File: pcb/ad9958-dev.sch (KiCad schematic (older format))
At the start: 120 parts, among them J1 5V, J2 HEAD-M10X2, J3 OUT0p, J4 OUT0n,1p, J5 15V, Q1 BFS17W, Q2 BFS17W, Q3 BFS17W, Q4 BFS17W, U1 LD1117V33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

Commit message: More schematic work - should be ready for layout
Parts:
- removed C31, C33, C34, C35, C40, C41, C42, C44, C48, C49, C50, C53, C54: 220n, IPC7351-Nominal:CAPC2012X70, symbol C-0805
- removed C39, C43, C45, C47, C51, C52: 1n, IPC7351-Nominal:CAPC1005X55, symbol C-0402
- removed C46: 47u, passive:C-ALUM-6.3mm, symbol C-ALUM-6.3mm
- removed D1: 1N5822, semi:DO-201, symbol 1N5822
- removed D2, D3: BAT54, IPC-semi-nominal:SOT-23, symbol BAT54
- removed E5, E6, E7, E8: 600, IPC7351-Nominal:INDC1005X60, symbol BEAD
- removed J2: HEAD-M10X2, conn:CONN_20-DIL, symbol HEAD-M10X2
- removed J5: 15V, conn:CONN_2-WIRES, symbol HEAD-M2
- removed JP1: SEL0n, conn:JUMPER-SOLDER-3, symbol JUMPER-SOLDER-3
- removed JP2: SEL1p, conn:JUMPER-SOLDER-3, symbol JUMPER-SOLDER-3
- removed MP1, MP2: 7-340-1PP-BA, symbol HEATSINK-NO-CONN
- removed Q1, Q2, Q3, Q4: BFS17W, IPC-semi-nominal:SOT-323, symbol BFS17W
- removed R15, R17: 220, IPC7351-Nominal:RESC1608X50, symbol R-0603
- removed R32: 3k3, IPC7351-Nominal:RESC1005X40, symbol R-0402
- removed R33: NP, IPC7351-Nominal:RESC1005X40, symbol R-0402
- removed R34, R35: 49r9, IPC7351-Nominal:RESC1005X40, symbol R-0402
- removed U1: LD1117V33, semi:TO-220, symbol LM1117-FIXED-TO220
- removed U2: LD1117V18, semi:TO-220, symbol LM1117-FIXED-TO220
- removed U4: LMV358, IPC7351-Nominal:SOP65P490X110-8B, symbol LMV358-MSOP
- added C31, C33, C35: 10n, symbol C-0402
- added C34: 100n, symbol C-0402
- added J2: 5V, symbol HEAD-F3
- added J5: HEAD-M10X2, symbol HEAD-M10X2
- added R15, R17: 49r9, symbol R-0402
- added U1: LM1117-FIXED-SOT223, symbol LM1117-FIXED-SOT223
- added U2, U4: LMH6714, symbol LMH6714-SOT23
- C29: value 1n -> 100n; footprint IPC7351-Nominal:CAPC1005X55 -> (none)
- C30, C36, C38: value 1n -> 10n; footprint IPC7351-Nominal:CAPC1005X55 -> (none)
- C32, C37: value 220n -> 10u; footprint IPC7351-Nominal:CAPC2012X70 -> (none)
- J1: value 5V -> 3V3
- J3: value OUT0p -> OUT0
- J4: value OUT0n,1p -> OUT1
- R13, R16: value 75 -> 49r9; footprint IPC7351-Nominal:RESC1005X40 -> (none)
- R18: value 360 -> 53r6; footprint IPC7351-Nominal:RESC1005X40 -> (none)
- R19: value 75 -> 53r6; footprint IPC7351-Nominal:RESC1005X40 -> (none)
- R20: value 3k3 -> 360; footprint IPC7351-Nominal:RESC1005X40 -> (none)
- R21: value 75 -> 360; footprint IPC7351-Nominal:RESC1005X40 -> (none)
- R22: value NP -> 360; footprint IPC7351-Nominal:RESC1005X40 -> (none)
- R23, R29, R30: value 10k -> 360; footprint IPC7351-Nominal:RESC1005X40 -> (none)
- R24: value 49r9 -> 2k2; footprint IPC7351-Nominal:RESC1005X40 -> (none)
- R25: value 10k -> 53r6; footprint IPC7351-Nominal:RESC1005X40 -> (none)
- R26: value 49r9 -> 53r6; footprint IPC7351-Nominal:RESC1005X40 -> (none)
- R27, R28: value 100 -> 360; footprint IPC7351-Nominal:RESC1005X40 -> (none)
- R31: value 360 -> 2k2; footprint IPC7351-Nominal:RESC1005X40 -> (none)
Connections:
- net labels added: +5, -5
- net labels removed: +15
- wire segments 334 -> 257
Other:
- note added: "4x 49r9"
- note added: "tline, Z0=50"
- note added: "tline, Z0=50, Zdiff=100"
- note removed: "75 OHM TLINE"
- moved on the sheet: J3

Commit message: PCB almost done
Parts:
- removed C11, C5: 47u, passive:C-ALUM-6.3mm, symbol C-ALUM-6.3mm
- removed C18, C26: 220n, IPC7351-Nominal:CAPC2012X70, symbol C-0805
- removed C33, C38: 10n, symbol C-0402
- removed J1: 3V3, conn:CONN_2-WIRES, symbol HEAD-M2
- added C33, C38: 10u, IPC7351-Nominal:CAPC2012X70, symbol C-0805
- added R32, R33: 49r9, IPC7351-Nominal:RESC1005X40, symbol R-0402
- C29, C30, C31, C34, C35, C36: footprint (none) -> IPC7351-Nominal:CAPC1005X55
- C32, C37: footprint (none) -> IPC7351-Nominal:CAPC2012X70
- J2: footprint (none) -> conn:CONN_3-SIL
- J5: footprint (none) -> conn:CONN_20-DIL
- R13, R15, R16, R17, R18, R19, R20, R21, R22, R23, R24, R25, R26, R27, R28, R29, R30, R31: footprint (none) -> IPC7351-Nominal:RESC1005X40
- U1: footprint (none) -> IPC-semi-nominal:SOT-223
- U2, U4: footprint (none) -> IPC-semi-nominal:SOT-23-5
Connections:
- net +1.8: no longer R13.1, R15.1, R16.1, R17.1, R18.1, R19.1, R25.1, R26.1
- net +1v8A: now also R13.1, R15.1, R16.1, R17.1, R18.1, R19.1, R25.1, R26.1
- net -5: now also C33.2, C38.2
- net GND: now also C33.1, C38.1
- net at R22.1, R24.1, U2.1 (OUT): now also R32.2; no longer J3.1
- net C0P: now reaches R25.2, R27.2
- net C0P: now also R13.2, U3.8 (CH0_IOUTp); no longer R16.2, U3.13 (CH1_IOUTp)
- net C0N: now reaches R26.2, R28.2
- net C0N: now also R15.2, U3.9 (CH0_IOUTn); no longer R17.2, U3.14 (CH2_IOUTn)
- net C1P: now reaches R18.2, R20.2
- net C1P: now also R16.2, U3.13 (CH1_IOUTp); no longer R13.2, U3.8 (CH0_IOUTp)
- net C1N: now reaches R19.2, R21.2
- net C1N: now also R17.2, U3.14 (CH2_IOUTn); no longer R15.2, U3.9 (CH0_IOUTn)
- net at E4.2: now also J5.20
- net at R1.2: now also J5.2; no longer J5.4
- net at R2.2: now also J5.16; no longer J5.6
- net at R3.2: now also J5.18; no longer J5.8
- net at R4.2: now also J5.4; no longer J5.10
- net at R5.2: now also J5.6; no longer J5.12
- net at R6.2: now also J5.8; no longer J5.14
- net at R7.2: now also J5.10; no longer J5.16
- net at R8.2: now also J5.12; no longer J5.18
- net at R9.2: now also J5.14; no longer J5.20
- net at R29.1, R31.1, U4.1 (OUT): now also R33.2; no longer J4.1
- new net: J3.1, R32.1
- new net: J4.1, R33.1
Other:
- note added: "tline, Z0=50, Zdiff=100\nOSH Park 4L: 0.3 track 0.7 space (1.0 align)"
- note removed: "tline, Z0=50, Zdiff=100"
- moved on the sheet: J3, J4, J5

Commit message: Added power protection, touched up PCB
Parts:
- added D1, D2, D3: SS12, IPC7351-Nominal:DIOM5326X292, symbol SS12
- added R34: 250mA, IPC7351-Nominal:RESC3216X60, symbol THERM
- added R35, R36: 100mA, IPC7351-Nominal:RESC3216X60, symbol THERM
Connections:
- net +3.3: now also D1.1, R34.2; no longer E4.1
- net +5: now also D2.1, R35.2; no longer E2.1
- net -5: now also D3.2, R36.2; no longer E3.1
- net GND: now also D1.2, D2.2, D3.1
- new net: E4.1, R34.1
- new net: E2.1, R35.1
- new net: E3.1, R36.1
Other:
- moved on the sheet: C12, C4, E2, E3, J2, U1

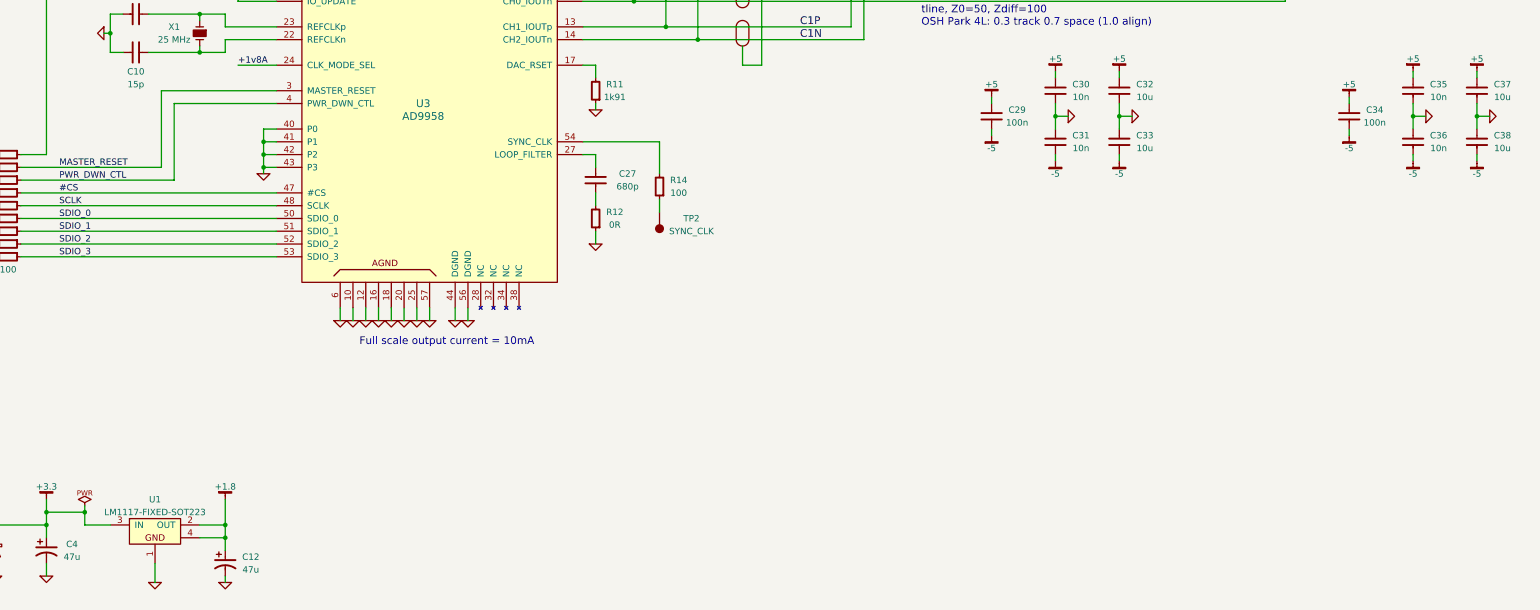
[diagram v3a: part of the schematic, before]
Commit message: Few part value changes
Added voltage to LDO
Changed 10nF to 1nF caps - eliminated BOM item
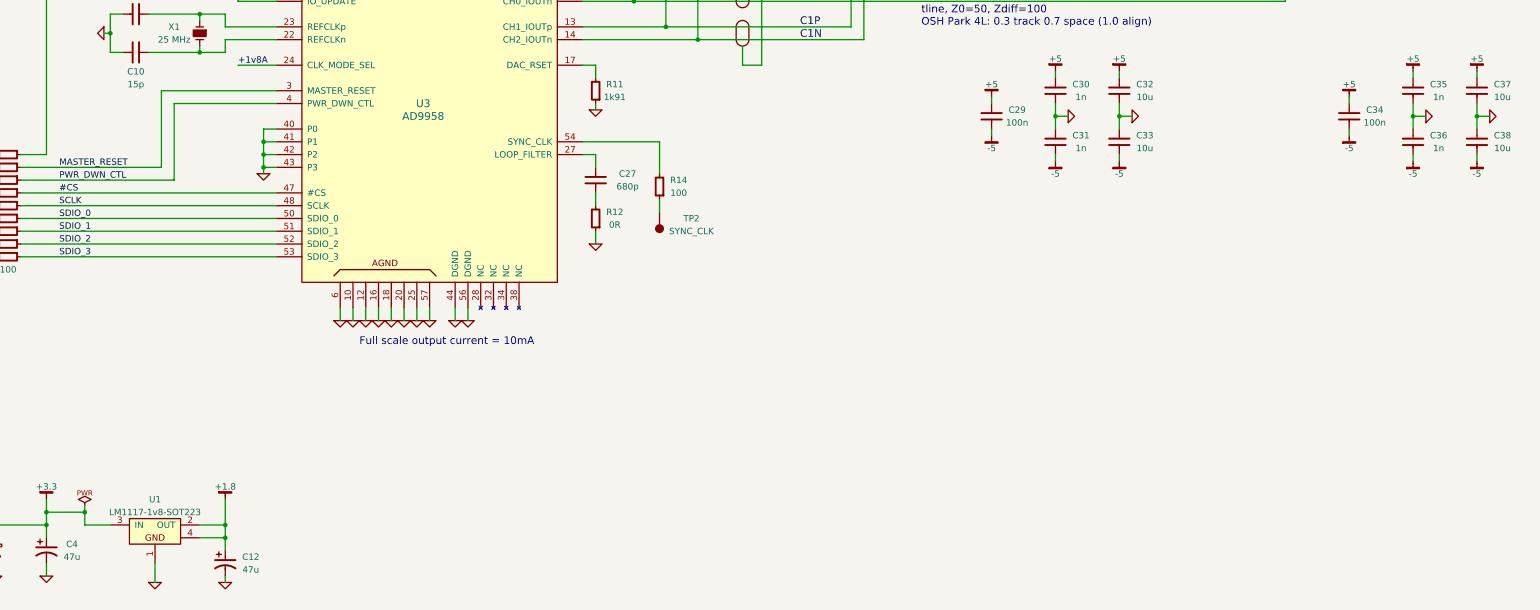
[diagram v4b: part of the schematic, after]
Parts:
- C30, C31, C35, C36: value 10n -> 1n
- U1: value LM1117-FIXED-SOT223 -> LM1117-1v8-SOT223
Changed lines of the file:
@@
 P 3350 8050
 F 0 "U1" H 3350 8300 50  0000 C CNN
-F 1 "LM1117-FIXED-SOT223" H 3350 8200 50  0000 C CNN
+F 1 "LM1117-1v8-SOT223" H 3350 8200 50  0000 C CNN
 F 2 "IPC-semi-nominal:SOT-223" H 3350 8050 60  0001 C CNN
 F 3 "" H 3350 8050 60  0000 C CNN
@@
 P 10400 4600
 F 0 "C30" H 10600 4650 50  0000 C CNN
-F 1 "10n" H 10600 4550 50  0000 C CNN
+F 1 "1n" H 10600 4550 50  0000 C CNN
 F 2 "IPC7351-Nominal:CAPC1005X55" H 10390 4575 60  0001 C CNN
 F 3 "" H 10390 4575 60  0000 C CNN
@@
 P 10400 5000
 F 0 "C31" H 10600 5050 50  0000 C CNN
-F 1 "10n" H 10600 4950 50  0000 C CNN
+F 1 "1n" H 10600 4950 50  0000 C CNN
 F 2 "IPC7351-Nominal:CAPC1005X55" H 10390 4975 60  0001 C CNN
 F 3 "" H 10390 4975 60  0000 C CNN
@@
 P 13200 4600
 F 0 "C35" H 13400 4650 50  0000 C CNN
-F 1 "10n" H 13400 4550 50  0000 C CNN
+F 1 "1n" H 13400 4550 50  0000 C CNN
 F 2 "IPC7351-Nominal:CAPC1005X55" H 13190 4575 60  0001 C CNN
 F 3 "" H 13190 4575 60  0000 C CNN
@@
 P 13200 5000
 F 0 "C36" H 13400 5050 50  0000 C CNN
-F 1 "10n" H 13400 4950 50  0000 C CNN
+F 1 "1n" H 13400 4950 50  0000 C CNN
 F 2 "IPC7351-Nominal:CAPC1005X55" H 13190 4975 60  0001 C CNN
 F 3 "" H 13190 4975 60  0000 C CNN

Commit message: Schematic touchups
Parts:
- J5: value HEAD-M10X2 -> INTERFACE
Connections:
- net +1v8A renamed +1.8A
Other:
- note added: "3v3 input"
- note added: "AD9958 DECOUPLING"
- note added: "OUTPUT AMP DECOUPLING"
- moved on the sheet: C1, C10, C12, C13, C14, C15, C16, C17, C19, C2, C20, C21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

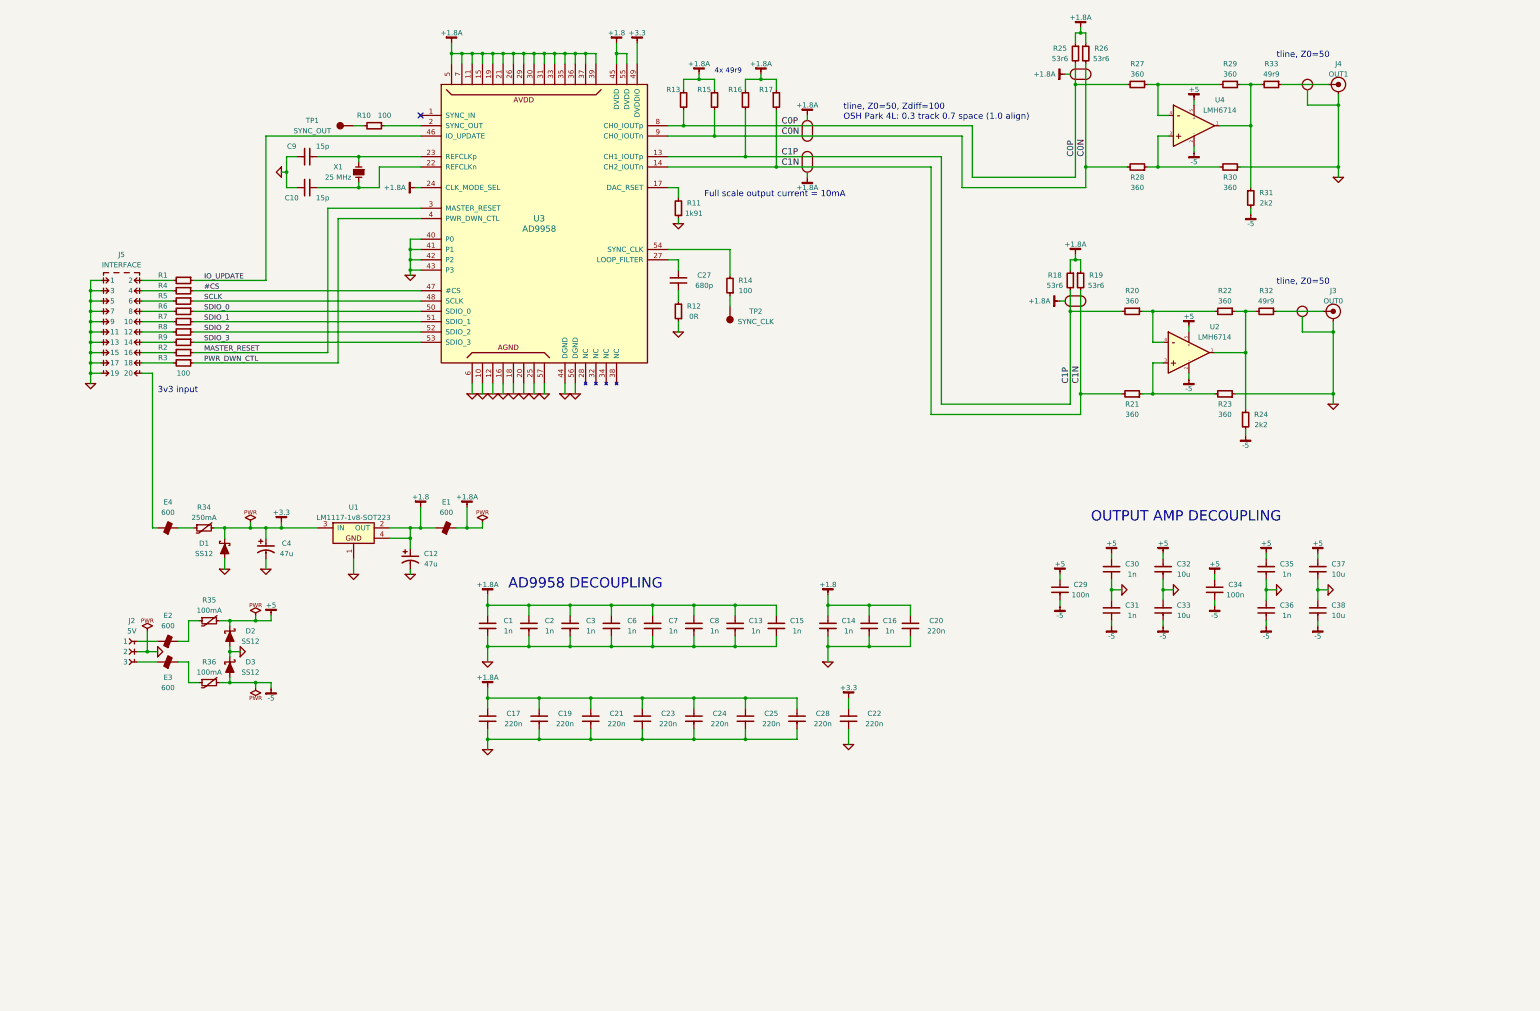
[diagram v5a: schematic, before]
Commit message: Reannotated components
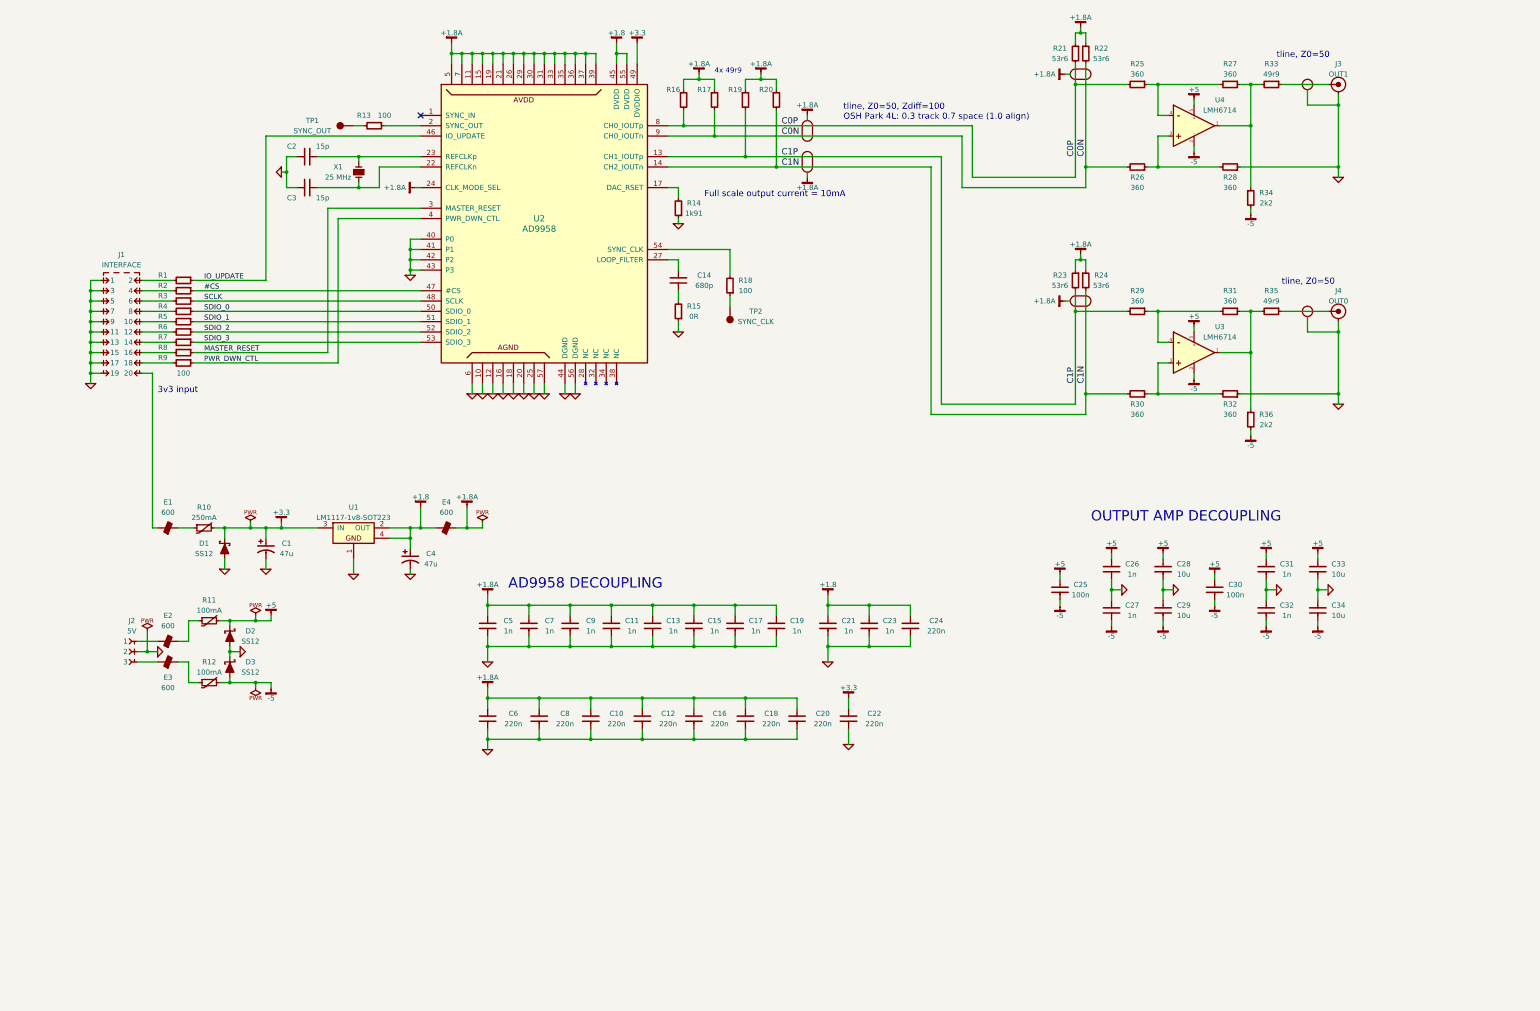
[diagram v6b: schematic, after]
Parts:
- C1: renamed from C4; OldReference (none) -> C4
- C10: renamed from C21; OldReference (none) -> C21
- C11: renamed from C6; OldReference (none) -> C6
- C12: renamed from C23; OldReference (none) -> C23
- C13: renamed from C7; OldReference (none) -> C7
- C14: renamed from C27; OldReference (none) -> C27
- C15: renamed from C8; OldReference (none) -> C8
- C16: renamed from C24; OldReference (none) -> C24
- C17: renamed from C13; OldReference (none) -> C13
- C18: renamed from C25; OldReference (none) -> C25
- C19: renamed from C15; OldReference (none) -> C15
- C2: renamed from C9; OldReference (none) -> C9
- C20: renamed from C28; OldReference (none) -> C28
- C21: renamed from C14; OldReference (none) -> C14
- C22: OldReference (none) -> C22
- C23: renamed from C16; OldReference (none) -> C16
- C24: renamed from C20; OldReference (none) -> C20
- C25: renamed from C29; OldReference (none) -> C29
- C26: renamed from C30; OldReference (none) -> C30
- C27: renamed from C31; OldReference (none) -> C31
- C28: renamed from C32; OldReference (none) -> C32
- C29: renamed from C33; OldReference (none) -> C33
- C3: renamed from C10; OldReference (none) -> C10
- C30: renamed from C34; OldReference (none) -> C34
- C31: renamed from C35; OldReference (none) -> C35
- C32: renamed from C36; OldReference (none) -> C36
- C33: renamed from C37; OldReference (none) -> C37
- C34: renamed from C38; OldReference (none) -> C38
- C4: renamed from C12; OldReference (none) -> C12
- C5: renamed from C1; OldReference (none) -> C1
- C6: renamed from C17; OldReference (none) -> C17
- C7: renamed from C2; OldReference (none) -> C2
- C8: renamed from C19; OldReference (none) -> C19
- C9: renamed from C3; OldReference (none) -> C3
- D1: OldReference (none) -> D1
- D2: OldReference (none) -> D2
- D3: OldReference (none) -> D3
- E1: renamed from E4; OldReference (none) -> E4
- E2: OldReference (none) -> E2
- E3: OldReference (none) -> E3
- E4: renamed from E1; OldReference (none) -> E1
- J1: renamed from J5; OldReference (none) -> J5
- J2: OldReference (none) -> J2
- J3: renamed from J4; OldReference (none) -> J4
- J4: renamed from J3; OldReference (none) -> J3
- R1: OldReference (none) -> R1
- R10: renamed from R34; OldReference (none) -> R34
- R11: renamed from R35; OldReference (none) -> R35
- R12: renamed from R36; OldReference (none) -> R36
- R13: renamed from R10; OldReference (none) -> R10
- R14: renamed from R11; OldReference (none) -> R11
- R15: renamed from R12; OldReference (none) -> R12
- R16: renamed from R13; OldReference (none) -> R13
- R17: renamed from R15; OldReference (none) -> R15
- R18: renamed from R14; OldReference (none) -> R14
- R19: renamed from R16; OldReference (none) -> R16
- R2: renamed from R4; OldReference (none) -> R4
- R20: renamed from R17; OldReference (none) -> R17
- R21: renamed from R25; OldReference (none) -> R25
- R22: renamed from R26; OldReference (none) -> R26
- R23: renamed from R18; OldReference (none) -> R18
- R24: renamed from R19; OldReference (none) -> R19
- R25: renamed from R27; OldReference (none) -> R27
- R26: renamed from R28; OldReference (none) -> R28
- R27: renamed from R29; OldReference (none) -> R29
- R28: renamed from R30; OldReference (none) -> R30
- R29: renamed from R20; OldReference (none) -> R20
- R3: renamed from R5; OldReference (none) -> R5
- R30: renamed from R21; OldReference (none) -> R21
- R31: renamed from R22; OldReference (none) -> R22
- R32: renamed from R23; OldReference (none) -> R23
- R33: OldReference (none) -> R33
- R34: renamed from R31; OldReference (none) -> R31
- R35: renamed from R32; OldReference (none) -> R32
- R36: renamed from R24; OldReference (none) -> R24
- R4: renamed from R6; OldReference (none) -> R6
- R5: renamed from R7; OldReference (none) -> R7
- R6: renamed from R8; OldReference (none) -> R8
- R7: renamed from R9; OldReference (none) -> R9
- R8: renamed from R2; OldReference (none) -> R2
- R9: renamed from R3; OldReference (none) -> R3
- TP1: OldReference (none) -> TP1
- TP2: OldReference (none) -> TP2
- U1: OldReference (none) -> U1
- U2: renamed from U3; OldReference (none) -> U3
- U3: renamed from U2; OldReference (none) -> U2
- U4: OldReference (none) -> U4
- X1: OldReference (none) -> X1
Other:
- moved on the sheet: J4, R23, R24, R29, R30, R31, R32, R35, R36, U3

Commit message: Prefab signoffs - CP
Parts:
- U1: value LM1117-1v8-SOT223 -> AZ1117CH-1.8TRG1
- U3, U4: value LMH6714 -> LMH6714MF
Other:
- note added: "2014-10-28 CP"
- note added: "ERC"
- note added: "Floating SYNC_IN is intentional.\nSee AD9958 datasheet page 29."
- note added: "PREFAB SIGNOFFS"
- note added: "Pin Connections"
- note added: "Pinouts"
